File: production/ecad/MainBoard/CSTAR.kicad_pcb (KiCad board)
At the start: 4 copper layers, 152.4 x 152.4 mm, 180 parts, among them IC1 LT8648SEV#PBF, J1 Conn_01x02_Pin, J10 Conn_01x03_Pin, J11 B4B-PH-K-S, J12 B4B-PH-K-S, J13 Conn_01x03_Pin, J13 Conn_01x05_Pin, J14 Conn_01x03_Pin, J15 Conn_01x03_Pin, J16 Conn_01x03_Pin, J17 Ultra_4, J18 Ultra_3, J19 Ultra_2, J2 Conn_01x02_Pin, J20 RX connect, J21 Ultra_1, J22 TX connect, J23 Conn_01x02_Pin, J24 Conn_01x02_Pin, J25 TYPE-C-31-M-12, J26 532610771, J28 532610771, J29 Conn_01x04_Socket, J3 Conn_01x02_Pin, J30 691137710002, J31 TYPE-C-31-M-12, J4 XT60PW-M, J5 Conn_01x02_Pin, J6 Conn_01x02_Pin, J7 532610771, J8 Conn_01x03_Pin, J9 Conn_01x03_Pin, Q1 AO3400A, Q2 AO3400A, Q3 AO3400A, Q4 AO3400A, Q5 AO3400A, Q6 AO3400A, Q7 AO3400A, Q8 IRFHM9331TRPBF, SW1 SW_Push, SW2 SW_Push, SW3 SW_Push, SW4 SW_Push, U1 AZ1117IH-3.3TRG1, U2 DRV8842PWPR, U3 DRV8842PWPR, U4 TXB0104DR, U5 CP2102N-A01-GQFN28, U6 ESP32-WROOM-32UE_M113EH6400UH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, U7 TXB0104DR, U8 CP2102N-A01-GQFN28, U9 ESP32-WROOM-32UE_M113EH6400UH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, X1 B2P-VH, X2 B2P-VH

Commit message: fixed some nets and MORE LAYOUT
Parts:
- moved C11 2.04 mm to (106.0, 176.8)
- moved R10 2.04 mm to (106.0, 173.8)
- moved R11 2.04 mm to (106.0, 179.9)
- moved R13 0.92 mm to (119.1, 90.8)
- moved C15 0.57 mm to (115.1, 90.9), turned to 90 degrees
- moved TP8 0.57 mm to (160.5, 90.2)
- moved TP9 0.25 mm to (123.4, 90.2)
- moved R12 0.15 mm to (156.0, 90.6)
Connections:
- U9 pad 13: Ch.B MOTOR 1 -> Ch.B_MOTOR_1
- U9 pad 14: OUT1 MOTOR 2 -> IN1_MOTOR_2
- U9 pad 16: Ch.A MOTOR 1 -> Ch.A_MOTOR_1
- U9 pad 23: Ch.A MOTOR 2 -> Ch.A_MOTOR_2
- U9 pad 24: OUT2 MOTOR 1 -> IN2_MOTOR_1
- U9 pad 26: OUT1 MOTOR 1 -> IN1_MOTOR_1
- U9 pad 29: OUT2 MOTOR 2 -> IN2_MOTOR_2
- U9 pad 30: Ch.B MOTOR 2 -> Ch.B_MOTOR_2
- U9 pad 4: nFAULT MOTOR 1 -> nFAULT_MOTOR_1
- U9 pad 7: nFAULT MOTOR 2 -> nFAULT_MOTOR_2
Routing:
- net GND: track 0.00 -> 59.6 mm, vias 0 -> 14
- net BATT_IN: track 0.00 -> 46.5 mm, vias 0 -> 1
- net +12V: track 0.00 -> 36.3 mm, vias 0 -> 4
- net Net-(IC1-EN/UV): track 0.00 -> 28.9 mm
- net Net-(IC1-SW_1): track 0.00 -> 17.6 mm
- net Net-(IC1-FB): track 0.00 -> 13.5 mm
- net Net-(IC1-RT): track 0.00 -> 8.12 mm
- net Net-(J1-Pin_2): track 0.00 -> 6.87 mm
- net Net-(IC1-VC): track 0.00 -> 5.47 mm
- net Net-(IC1-INTVCC): track 0.00 -> 4.97 mm
- net Net-(IC1-SYNC/MODE): track 0.00 -> 4.85 mm
- net Net-(C38-Pad1): track 0.00 -> 4.51 mm
- net Net-(C3-Pad1): track 0.00 -> 3.06 mm
- net +24V: track 0.00 -> 2.08 mm
- net Net-(LED2-Pad2): track 0.00 -> 2.03 mm
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- added copper zone on In2.Cu, net +12V
- added copper zone on In1.Cu, net GND

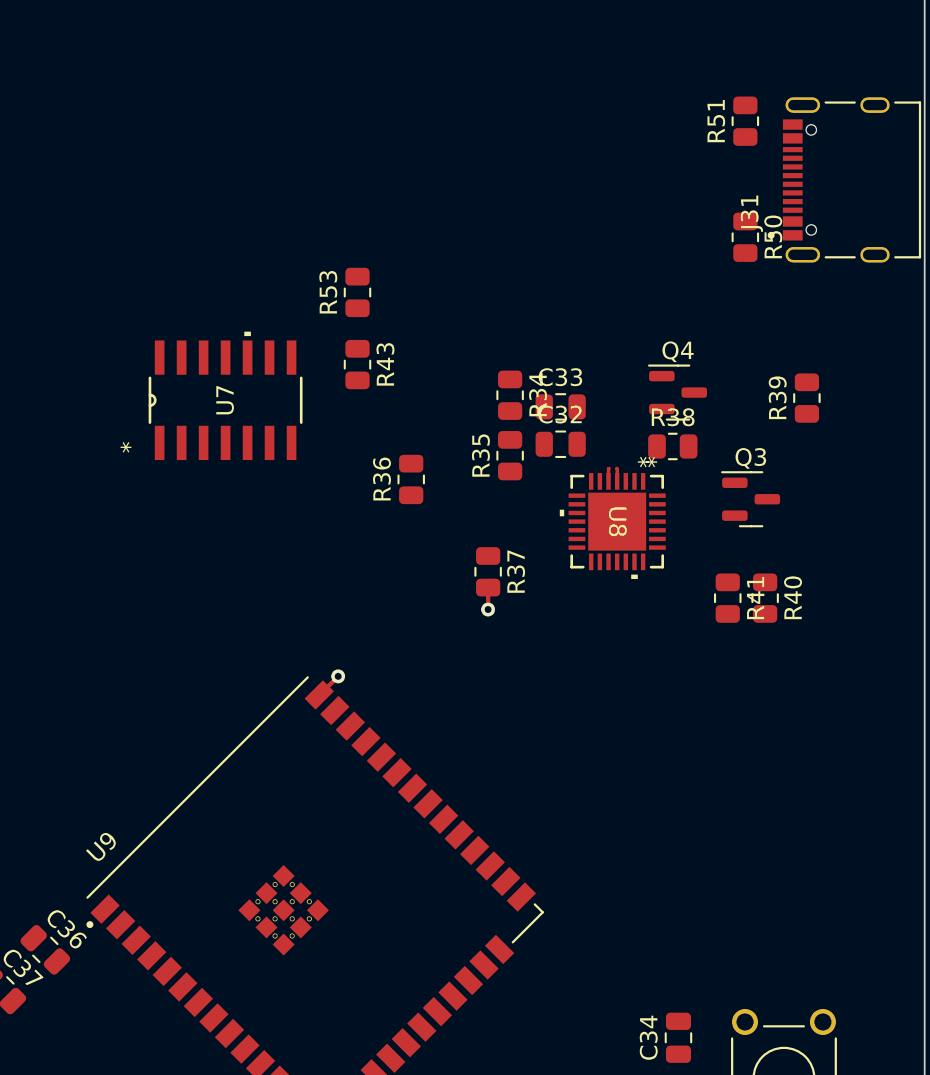
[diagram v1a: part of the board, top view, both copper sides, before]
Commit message: "Finished Routing ESP to Bootloading"
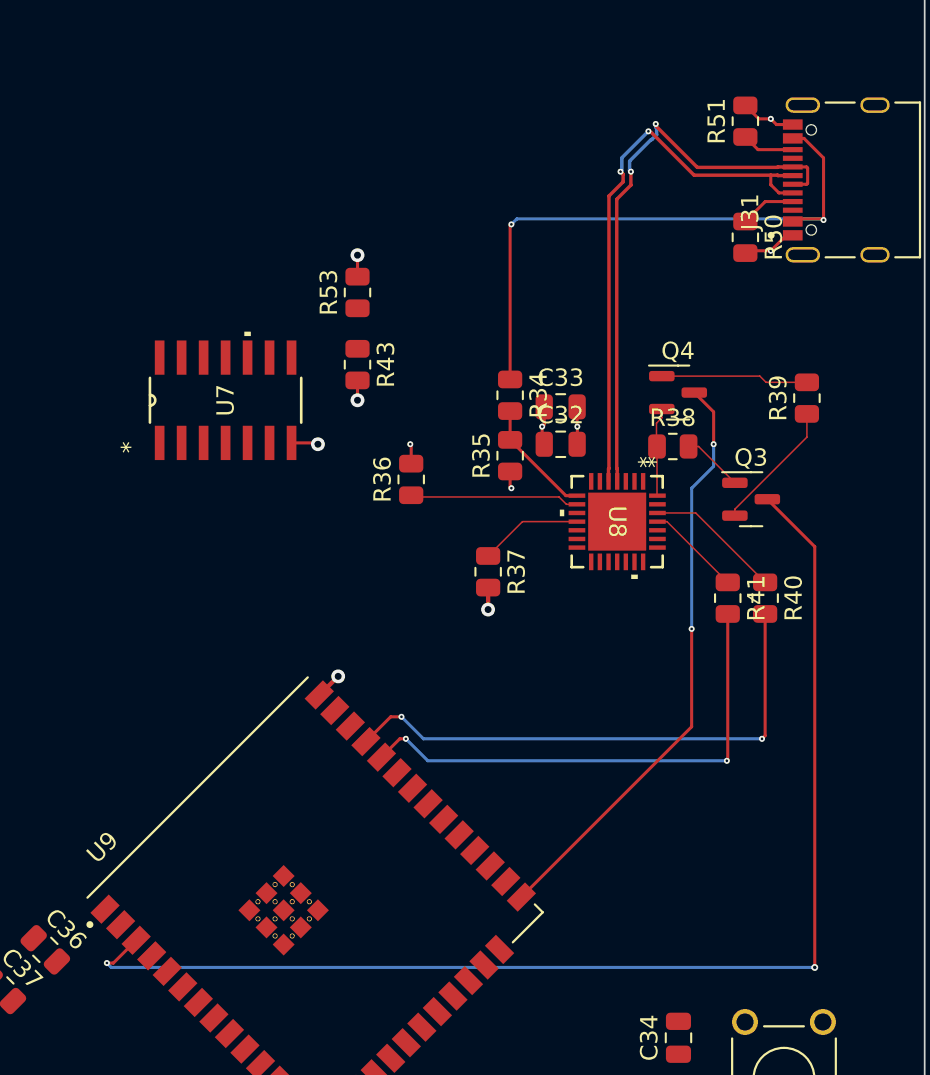
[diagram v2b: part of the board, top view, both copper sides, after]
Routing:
- net EN_2: track 0.00 -> 71.4 mm, vias 0 -> 2
- net VBUS_2: track 0.00 -> 34.9 mm, vias 0 -> 2
- net IO0_2: track 0.00 -> 34.2 mm, vias 0 -> 2
- net USB2_D+: track 0.76 -> 33.9 mm, vias 0 -> 2
- net USB2_D-: track 0.76 -> 33.2 mm, vias 0 -> 2
- net UART_TXD_2: track 0.00 -> 31.3 mm, vias 0 -> 2
- net UART_RXD_2: track 0.00 -> 29.4 mm, vias 0 -> 2
- net GND: track 59.6 -> 72.0 mm, vias 14 -> 20
- net Net-(U8-RSTb): track 0.00 -> 9.79 mm
- net Net-(Q4-G): track 0.00 -> 8.53 mm
- net Net-(U8-TXD): track 0.00 -> 7.88 mm
- net RTS_2: track 0.00 -> 7.60 mm
- net Net-(U8-VBUS): track 0.00 -> 6.86 mm
- net Net-(U8-SUSPENDb): track 0.00 -> 5.95 mm
- net Net-(U8-RXD): track 0.00 -> 5.52 mm
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
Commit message: Lots of power routing and power planes!
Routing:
- net +5V: track 0.00 -> 49.5 mm, vias 0 -> 2
- net (no net): track 0.00 -> 27.1 mm, vias 4 -> 2
- net Net-(C38-Pad1): track 4.51 -> 31.1 mm
- net GND: track 72.0 -> 95.0 mm, vias 20 -> 34
- net +3V3: track 3.31 -> 22.8 mm
- net Net-(J2-Pin_1): track 0.00 -> 18.0 mm
- net Net-(J3-Pin_1): track 0.00 -> 15.5 mm
- net Net-(PS1-FB): track 0.00 -> 13.5 mm
- net Net-(PS1-SW): track 0.00 -> 13.0 mm
- net Net-(J23-Pin_2): track 0.00 -> 7.17 mm
- net Net-(J30-Pad1): track 0.00 -> 6.86 mm
- net USB2_D-: track 33.2 -> 38.9 mm
- net Net-(J3-Pin_2): track 0.00 -> 4.46 mm
- net Net-(J2-Pin_2): track 0.00 -> 3.99 mm
- net USB2_D+: track 33.9 -> 37.9 mm
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- added copper zone on In2.Cu, net +3V3
- added copper zone on In2.Cu, net +5V

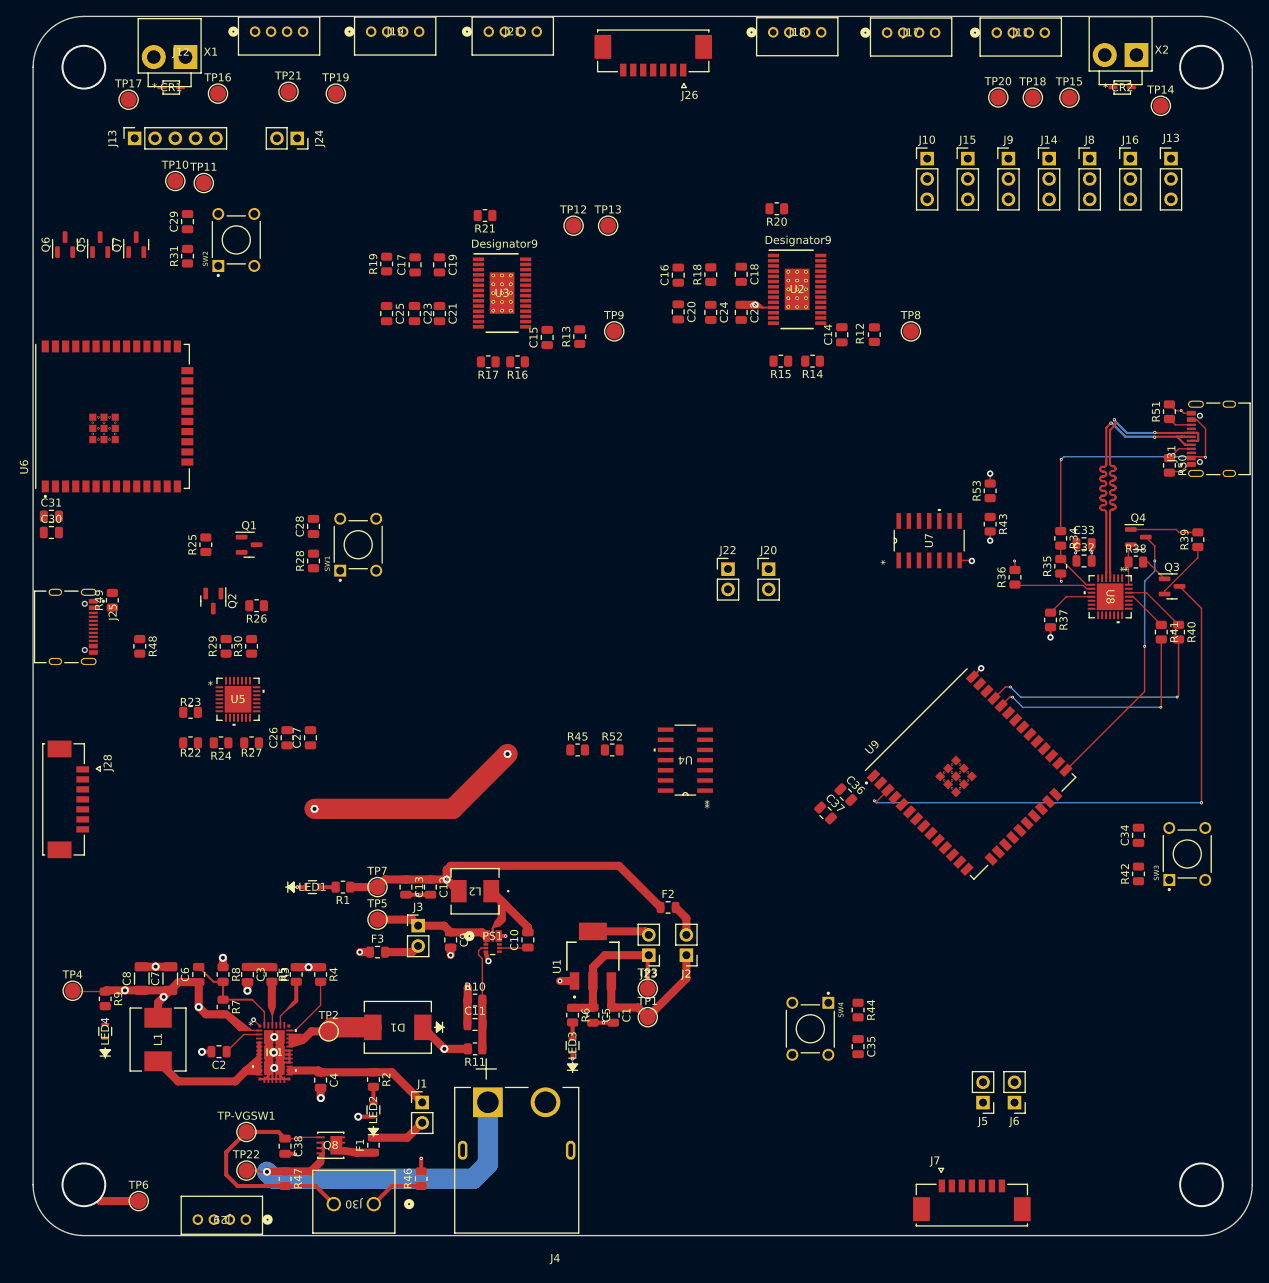
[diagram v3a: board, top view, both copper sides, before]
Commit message: " I routed one net while drinking for the st. pattys pregame sorry"
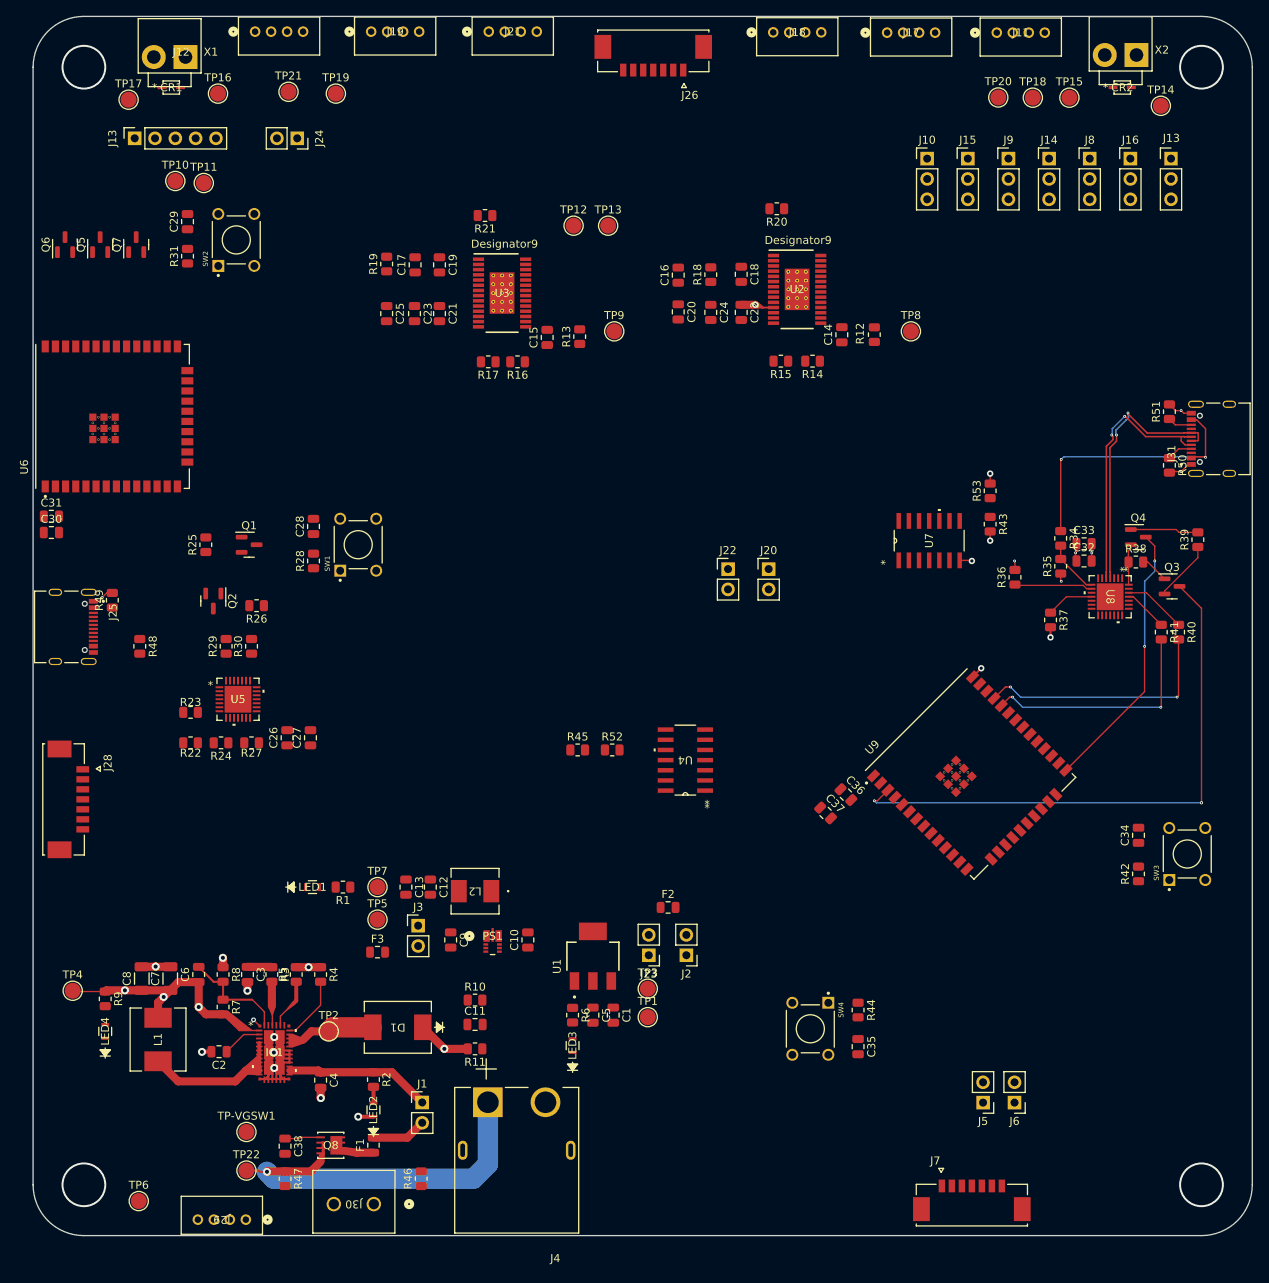
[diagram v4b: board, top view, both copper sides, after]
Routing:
- net +5V: track 49.5 -> 0.00 mm, vias 2 -> 0
- net (no net): track 27.1 -> 0.00 mm, vias 2 -> 4
- net Net-(C38-Pad1): track 31.1 -> 4.51 mm
- net GND: track 95.0 -> 74.9 mm, vias 34 -> 21
- net +3V3: track 22.8 -> 3.31 mm
- net Net-(J2-Pin_1): track 18.0 -> 0.00 mm
- net Net-(J3-Pin_1): track 15.5 -> 0.00 mm
- net Net-(PS1-FB): track 13.5 -> 0.00 mm
- net Net-(PS1-SW): track 13.0 -> 0.00 mm
- net Net-(J23-Pin_2): track 7.17 -> 0.00 mm
- net Net-(J30-Pad1): track 6.86 -> 0.00 mm
- net USB2_D-: track 38.9 -> 33.2 mm
- net Net-(J3-Pin_2): track 4.46 -> 0.00 mm
- net Net-(J2-Pin_2): track 3.99 -> 0.00 mm
- net USB2_D+: track 37.9 -> 33.9 mm
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- removed copper zone on In2.Cu, net +3V3
- removed copper zone on In2.Cu, net +5V

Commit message: "Hehe i routed another net"
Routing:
- net GND: track 74.9 -> 76.0 mm, vias 21 -> 22
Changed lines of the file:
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@@
   (segment (start 60.0105 122.8695) (end 59.436 123.444) (width 0.1778) (layer "F.Cu") (net 2))
   (segment (start 71.9328 180.213) (end 71.9074 180.2384) (width 0.508) (layer "F.Cu") (net 2))
+  (segment (start 64.135 131.445) (end 64.008 131.572) (width 0.1778) (layer "F.Cu") (net 2))
   (segment (start 81.711165 183.718708) (end 81.711165 182.295165) (width 0.254) (layer "F.Cu") (net 2))
   (segment (start 81.211039 183.718708) (end 81.211039 182.694961) (width 0.254) (layer "F.Cu") (net 2))
+  (segment (start 64.135 130.4525) (end 64.135 131.445) (width 0.1778) (layer "F.Cu") (net 2))
   (segment (start 82.853276 180.065045) (end 81.149063 180.065045) (width 0.254) (layer "F.Cu") (net 2))
   (segment (start 73.091 180.213) (end 71.9328 180.213) (width 0.508) (layer "F.Cu") (net 2))
@@
   (via (at 102.2096 179.8574) (size 1) (drill 0.5) (layers "F.Cu" "B.Cu") (net 2))
   (via (at 170.434 116.332) (size 0.8) (drill 0.4) (layers "F.Cu" "B.Cu") (net 2))
+  (via (at 64.008 131.572) (size 0.35) (drill 0.15) (layers "F.Cu" "B.Cu") (net 2))
   (segment (start 77.139459 178.064541) (end 79.068676 178.064541) (width 0.1778) (layer "F.Cu") (net 3))
   (segment (start 74.991 180.213) (end 77.139459 178.064541) (width 0.1778) (layer "F.Cu") (net 3))

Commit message: "Another one"
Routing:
- net GND: track 76.0 -> 77.2 mm, vias 22 -> 23
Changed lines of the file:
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@@
   (segment (start 82.853276 181.065297) (end 81.649189 181.065297) (width 0.254) (layer "F.Cu") (net 2))
   (segment (start 82.149315 181.565423) (end 80.899 180.315108) (width 0.254) (layer "F.Cu") (net 2))
+  (segment (start 58.3325 130.312) (end 59.426 130.312) (width 0.1778) (layer "F.Cu") (net 2))
   (segment (start 81.661 180.315108) (end 80.899 180.315108) (width 1.016) (layer "F.Cu") (net 2))
   (segment (start 80.260952 183.168417) (end 80.260952 182.245) (width 0.254) (layer "F.Cu") (net 2))
@@
   (segment (start 59.436 123.444) (end 59.436 123.571) (width 0.1778) (layer "F.Cu") (net 2))
   (segment (start 79.710661 183.718708) (end 80.260952 183.168417) (width 0.254) (layer "F.Cu") (net 2))
+  (segment (start 59.426 130.312) (end 59.436 130.302) (width 0.1778) (layer "F.Cu") (net 2))
   (segment (start 81.149063 180.565171) (end 80.899 180.315108) (width 0.254) (layer "F.Cu") (net 2))
   (segment (start 81.649189 181.065297) (end 80.899 180.315108) (width 0.254) (layer "F.Cu") (net 2))
@@
   (via (at 194.31 100.076) (size 0.35) (drill 0.15) (layers "F.Cu" "B.Cu") (net 2))
   (via (at 80.9498 182.245) (size 1) (drill 0.5) (layers "F.Cu" "B.Cu") (net 2))
+  (via (at 59.436 130.302) (size 0.35) (drill 0.15) (layers "F.Cu" "B.Cu") (net 2))
   (via (at 80.899 180.315108) (size 1) (drill 0.5) (layers "F.Cu" "B.Cu") (net 2))
   (via (at 71.9074 180.2384) (size 1) (drill 0.5) (layers "F.Cu" "B.Cu") (net 2))
